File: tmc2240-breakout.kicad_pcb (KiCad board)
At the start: 2 copper layers, 69 x 51 mm, 0 parts

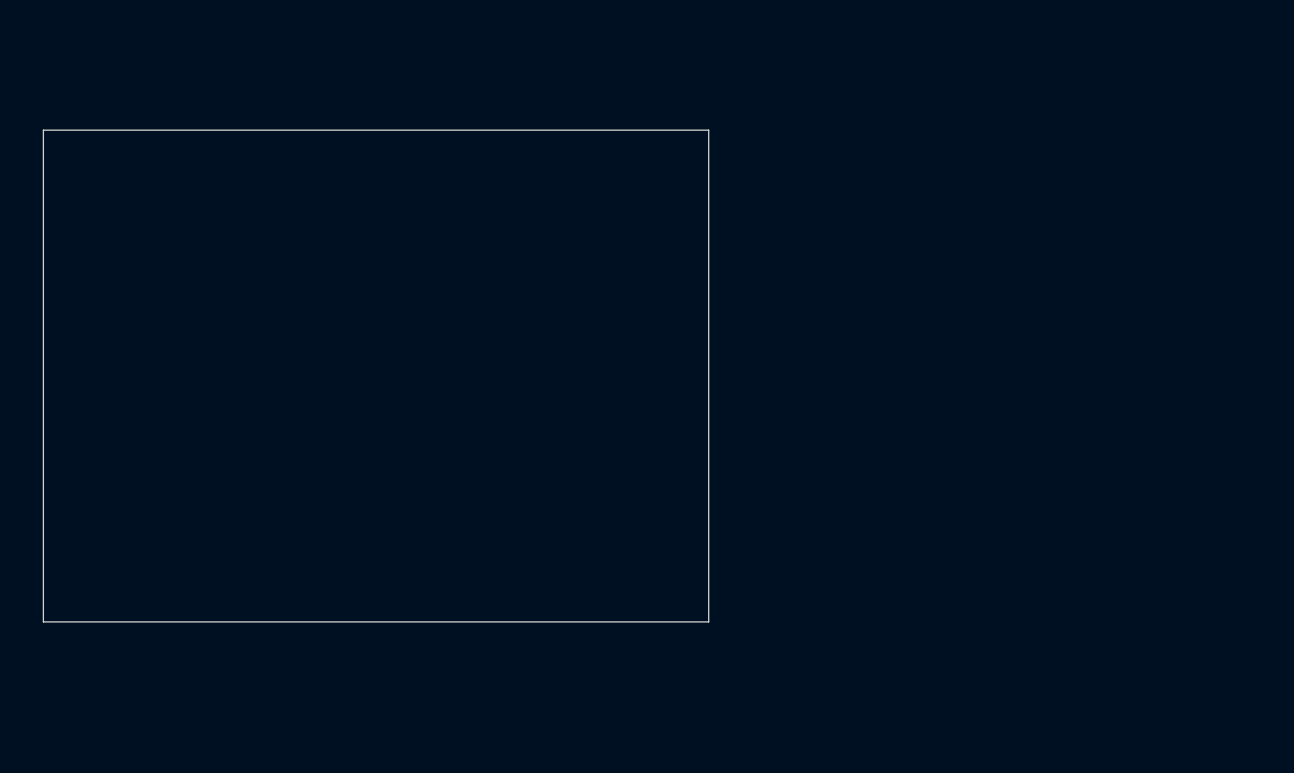
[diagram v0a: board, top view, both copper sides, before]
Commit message: did some pcb placement
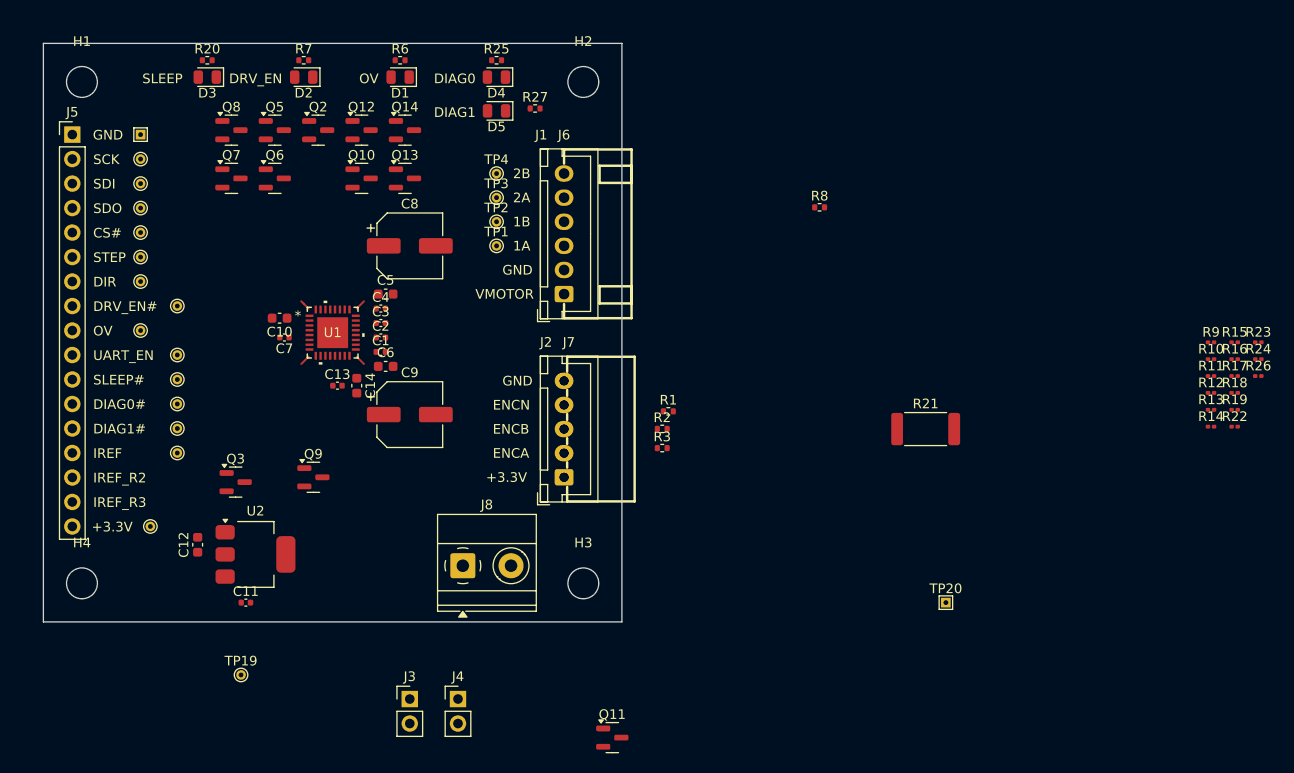
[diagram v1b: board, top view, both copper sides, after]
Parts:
- added C1: 100nF 50V, Capacitor_SMD:C_0402_1005Metric, F.Cu at (151.0, 92.0)
- added C10: 2.2uF 16V, Capacitor_SMD:C_0603_1608Metric, F.Cu at (140.5, 88.5)
- added C11: 100nF 50V, Capacitor_SMD:C_0402_1005Metric, F.Cu at (137.0, 118.0)
- added C12: 10uF 10V, Capacitor_SMD:C_0603_1608Metric, F.Cu at (132.0, 112.0)
- added C13: 22nF 50V, Capacitor_SMD:C_0402_1005Metric, F.Cu at (146.5, 95.5)
- added C14: 1uF 50V, Capacitor_SMD:C_0603_1608Metric, F.Cu at (148.5, 95.5)
- added C2: 100nF 50V, Capacitor_SMD:C_0402_1005Metric, F.Cu at (151.0, 90.5)
- added C3: 100nF 50V, Capacitor_SMD:C_0402_1005Metric, F.Cu at (151.0, 89.0)
- added C4: 100nF 50V, Capacitor_SMD:C_0402_1005Metric, F.Cu at (151.0, 87.5)
- added C5: 1uF 50V, Capacitor_SMD:C_0603_1608Metric, F.Cu at (151.5, 86.0)
- added C6: 1uF 50V, Capacitor_SMD:C_0603_1608Metric, F.Cu at (151.5, 93.5)
- added C7: 100nF 50V, Capacitor_SMD:C_0402_1005Metric, F.Cu at (141.0, 90.5)
- added C8: 47uF 63V, Capacitor_SMD:CP_Elec_6.3x7.7, F.Cu at (154.0, 81.0)
- added C9: 47uF 63V, Capacitor_SMD:CP_Elec_6.3x7.7, F.Cu at (154.0, 98.5)
- added D1: RED, LED_SMD:LED_0805_2012Metric, F.Cu at (153.0, 63.5)
- added D2: GREEN, LED_SMD:LED_0805_2012Metric, F.Cu at (143.0, 63.5)
- added D3: WHITE, LED_SMD:LED_0805_2012Metric, F.Cu at (133.0, 63.5)
- added D4: RED, LED_SMD:LED_0805_2012Metric, F.Cu at (163.0, 63.5)
- added D5: RED, LED_SMD:LED_0805_2012Metric, F.Cu at (163.0, 67.0)
- added H1: MountingHole, MountingHole:MountingHole_3.2mm_M3, F.Cu at (120.0, 64.0)
- added H2: MountingHole, MountingHole:MountingHole_3.2mm_M3, F.Cu at (172.0, 64.0)
- added H3: MountingHole, MountingHole:MountingHole_3.2mm_M3, F.Cu at (172.0, 116.0)
- added H4: MountingHole, MountingHole:MountingHole_3.2mm_M3, F.Cu at (120.0, 116.0)
- added J1: Conn_01x06, XH-W-6A:CONN-TH_6P-P2.50_DEALON_XH-W-6A, F.Cu at (170.0, 79.8)
- added J2: Conn_01x05, HDGC2501WR-5P:CONN-TH_5P-P2.50_HDGC2501WR-5P, F.Cu at (170.0, 100.0)
- added J3: Conn_01x02, Connector_PinHeader_2.54mm:PinHeader_1x02_P2.54mm_Vertical, F.Cu at (154.0, 128.0)
- added J4: Conn_01x02, Connector_PinHeader_2.54mm:PinHeader_1x02_P2.54mm_Vertical, F.Cu at (159.0, 128.0)
- added J5: Conn_01x17, Connector_PinHeader_2.54mm:PinHeader_1x17_P2.54mm_Vertical, F.Cu at (119.0, 69.5)
- added J6: Conn_01x06, Connector_JST:JST_XH_B6B-XH-A_1x06_P2.50mm_Vertical, F.Cu at (170.0, 86.0)
- added J7: Conn_01x05, Connector_JST:JST_XH_B5B-XH-A_1x05_P2.50mm_Vertical, F.Cu at (170.0, 105.0)
- added J8: Conn_01x02, TerminalBlock_Phoenix:TerminalBlock_Phoenix_MKDS-1,5-2_1x02_P5.00mm_Horizontal, F.Cu at (159.5, 114.2)
- added Q10: 2N7002, Package_TO_SOT_SMD:SOT-23, F.Cu at (149.0, 74.0)
- added Q11: 2N7002, Package_TO_SOT_SMD:SOT-23, F.Cu at (175.0, 132.0)
- added Q12: 2N7002, Package_TO_SOT_SMD:SOT-23, F.Cu at (149.0, 69.0)
- added Q13: 2N7002, Package_TO_SOT_SMD:SOT-23, F.Cu at (153.5, 74.0)
- added Q14: 2N7002, Package_TO_SOT_SMD:SOT-23, F.Cu at (153.5, 69.0)
- added Q2: 2N7002, Package_TO_SOT_SMD:SOT-23, F.Cu at (144.5, 69.0)
- added Q3: 2N7002, Package_TO_SOT_SMD:SOT-23, F.Cu at (135.9, 105.5)
- added Q5: 2N7002, Package_TO_SOT_SMD:SOT-23, F.Cu at (140.0, 69.0)
- added Q6: 2N7002, Package_TO_SOT_SMD:SOT-23, F.Cu at (140.0, 74.0)
- added Q7: 2N7002, Package_TO_SOT_SMD:SOT-23, F.Cu at (135.5, 74.0)
- added Q8: 2N7002, Package_TO_SOT_SMD:SOT-23, F.Cu at (135.5, 69.0)
- added Q9: 2N7002, Package_TO_SOT_SMD:SOT-23, F.Cu at (144.0, 105.0)
- added R1: 100k, Resistor_SMD:R_0402_1005Metric, F.Cu at (180.8, 98.2)
- added R10: 24k, Resistor_SMD:R_0201_0603Metric, F.Cu at (237.1, 92.8)
- added R11: 24k, Resistor_SMD:R_0201_0603Metric, F.Cu at (237.1, 94.5)
- added R12: 24k, Resistor_SMD:R_0201_0603Metric, F.Cu at (237.1, 96.2)
- added R13: 24k, Resistor_SMD:R_0201_0603Metric, F.Cu at (237.1, 98.0)
- added R14: 24k, Resistor_SMD:R_0201_0603Metric, F.Cu at (237.1, 99.8)
- added R15: 24k, Resistor_SMD:R_0201_0603Metric, F.Cu at (239.6, 91.0)
- added R16: 24k, Resistor_SMD:R_0201_0603Metric, F.Cu at (239.6, 92.8)
- added R17: 24k, Resistor_SMD:R_0201_0603Metric, F.Cu at (239.6, 94.5)
- added R18: 24k, Resistor_SMD:R_0201_0603Metric, F.Cu at (239.6, 96.2)
- added R19: 24k, Resistor_SMD:R_0201_0603Metric, F.Cu at (239.6, 98.0)
- added R2: 100k, Resistor_SMD:R_0402_1005Metric, F.Cu at (180.2, 100.0)
- added R20: 22, Resistor_SMD:R_0402_1005Metric, F.Cu at (133.0, 61.8)
- added R21: 1.8k, Resistor_SMD:R_2512_6332Metric, F.Cu at (207.5, 100.0)
- added R22: 24k, Resistor_SMD:R_0201_0603Metric, F.Cu at (239.6, 99.8)
- added R23: 24k, Resistor_SMD:R_0201_0603Metric, F.Cu at (242.0, 91.0)
- added R24: 24k, Resistor_SMD:R_0201_0603Metric, F.Cu at (242.0, 92.8)
- added R25: 33, Resistor_SMD:R_0402_1005Metric, F.Cu at (163.0, 61.8)
- added R26: 24k, Resistor_SMD:R_0201_0603Metric, F.Cu at (242.0, 94.5)
- added R27: 33, Resistor_SMD:R_0402_1005Metric, F.Cu at (167.0, 66.8)
- added R3: 100k, Resistor_SMD:R_0402_1005Metric, F.Cu at (180.2, 102.0)
- added R6: 33, Resistor_SMD:R_0402_1005Metric, F.Cu at (153.0, 61.8)
- added R7: 33, Resistor_SMD:R_0402_1005Metric, F.Cu at (143.0, 61.8)
- added R8: 100k, Resistor_SMD:R_0402_1005Metric, F.Cu at (196.5, 77.0)
- added R9: 24k, Resistor_SMD:R_0201_0603Metric, F.Cu at (237.1, 91.0)
- added TP1: TestPoint, TestPoint:TestPoint_THTPad_D1.0mm_Drill0.5mm, F.Cu at (163.0, 81.0)
- added TP10: TestPoint, TestPoint:TestPoint_THTPad_D1.0mm_Drill0.5mm, F.Cu at (126.1, 84.7)
- added TP11: TestPoint, TestPoint:TestPoint_THTPad_D1.0mm_Drill0.5mm, F.Cu at (129.9, 87.2)
- added TP12: TestPoint, TestPoint:TestPoint_THTPad_D1.0mm_Drill0.5mm, F.Cu at (126.1, 89.8)
- added TP13: TestPoint, TestPoint:TestPoint_THTPad_D1.0mm_Drill0.5mm, F.Cu at (129.9, 92.3)
- added TP14: TestPoint, TestPoint:TestPoint_THTPad_D1.0mm_Drill0.5mm, F.Cu at (129.9, 94.9)
- added TP15: TestPoint, TestPoint:TestPoint_THTPad_D1.0mm_Drill0.5mm, F.Cu at (129.9, 97.4)
- added TP16: TestPoint, TestPoint:TestPoint_THTPad_D1.0mm_Drill0.5mm, F.Cu at (129.9, 99.9)
- added TP17: TestPoint, TestPoint:TestPoint_THTPad_D1.0mm_Drill0.5mm, F.Cu at (129.9, 102.5)
- added TP18: TestPoint, TestPoint:TestPoint_THTPad_D1.0mm_Drill0.5mm, F.Cu at (127.1, 110.1)
- added TP19: TestPoint, TestPoint:TestPoint_THTPad_D1.0mm_Drill0.5mm, F.Cu at (136.5, 125.5)
- added TP2: TestPoint, TestPoint:TestPoint_THTPad_D1.0mm_Drill0.5mm, F.Cu at (163.0, 78.5)
- added TP20: TestPoint_Alt, TestPoint:TestPoint_THTPad_1.0x1.0mm_Drill0.5mm, F.Cu at (209.6, 118.0)
- added TP21: TestPoint_Alt, TestPoint:TestPoint_THTPad_1.0x1.0mm_Drill0.5mm, F.Cu at (126.1, 69.5)
- added TP3: TestPoint, TestPoint:TestPoint_THTPad_D1.0mm_Drill0.5mm, F.Cu at (163.0, 76.0)
- added TP4: TestPoint, TestPoint:TestPoint_THTPad_D1.0mm_Drill0.5mm, F.Cu at (163.0, 73.5)
- added TP5: TestPoint, TestPoint:TestPoint_THTPad_D1.0mm_Drill0.5mm, F.Cu at (126.1, 72.0)
- added TP6: TestPoint, TestPoint:TestPoint_THTPad_D1.0mm_Drill0.5mm, F.Cu at (126.1, 74.5)
- added TP7: TestPoint, TestPoint:TestPoint_THTPad_D1.0mm_Drill0.5mm, F.Cu at (126.1, 77.1)
- added TP8: TestPoint, TestPoint:TestPoint_THTPad_D1.0mm_Drill0.5mm, F.Cu at (126.1, 79.6)
- added TP9: TestPoint, TestPoint:TestPoint_THTPad_D1.0mm_Drill0.5mm, F.Cu at (126.1, 82.2)
- added U1: TMC2240ATJ+, ul_TMC2240ATJ-:21-0140_T3255&plus_5C_TRI, F.Cu at (146.0, 90.0)
- added U2: LD1117S18TR_SOT223, Package_TO_SOT_SMD:SOT-223-3_TabPin2, F.Cu at (138.0, 113.0)
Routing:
- net (no net): track 0.00 -> 4.24 mm
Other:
- board size 69 x 51 mm -> 60 x 60 mm
- board text added: "+3.3V"
- board text added: "1A"
- board text added: "1B"
- board text added: "2A"
- board text added: "2B"
- board text added: "CS#"
- board text added: "DIAG0"
- board text added: "DIAG0#"
- board text added: "DIAG1"
- board text added: "DIAG1#"
- board text added: "DIR"
- board text added: "DRV_EN"
- board text added: "DRV_EN#"
- board text added: "ENCA"
- board text added: "ENCB"
- board text added: "ENCN"
- board text added: "GND"
- board text added: "IREF"
- board text added: "IREF_R2"
- board text added: "IREF_R3"
- board text added: "OV"
- board text added: "SCK"
- board text added: "SDI"
- board text added: "SDO"
- board text added: "SLEEP"
- board text added: "SLEEP#"
- board text added: "STEP"
- board text added: "UART_EN"
- board text added: "VMOTOR"

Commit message: did some more placements
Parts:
- moved R19 110.0 mm to (132.2, 74.0)
- moved R12 104.1 mm to (133.0, 94.8), turned to 180 degrees
- moved R9 104.1 mm to (133.0, 89.8), turned to 180 degrees
- moved R11 104.1 mm to (133.0, 93.5)
- moved R10 104.1 mm to (133.0, 92.2), turned to 180 degrees
- moved R26 98.6 mm to (145.8, 73.0)
- moved R24 98.1 mm to (145.8, 74.0)
- moved R18 96.2 mm to (145.8, 75.0)
- moved R23 94.2 mm to (149.5, 109.0), turned to 90 degrees
- moved R16 91.8 mm to (148.8, 106.0), turned to 90 degrees
- moved R15 89.6 mm to (151.2, 106.0), turned to -90 degrees
- moved R13 87.5 mm to (150.0, 106.0), turned to -90 degrees
- moved R17 86.6 mm to (153.8, 106.0), turned to -90 degrees
- moved R14 84.8 mm to (152.5, 106.0), turned to -90 degrees
- moved R22 84.6 mm to (155.5, 109.0), turned to 90 degrees
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
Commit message: started doing some routing
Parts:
- moved R12 21.8 mm to (132.2, 73.0), turned to 0 degrees
- moved R9 11.2 mm to (133.0, 101.0)
- moved TP19 10.7 mm to (133.5, 107.1)
- moved C5 8.51 mm to (151.0, 94.5)
- moved C6 8.02 mm to (151.0, 85.5)
- moved C9 5.30 mm to (157.8, 102.2), turned to 180 degrees
- moved C8 5.15 mm to (149.0, 79.8)
- moved TP11 3.78 mm to (126.1, 87.2)
- moved R8 3.21 mm to (133.0, 90.2)
- moved R3 2.40 mm to (163.7, 90.5)
- moved TP5 1.81 mm to (127.9, 72.0)
- moved R1 1.30 mm to (165.1, 90.5)
- moved C1 1.15 mm to (151.0, 93.2)
- moved R10 0.71 mm to (133.0, 93.0)
- moved R11 0.71 mm to (133.0, 94.2)
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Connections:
- J1 pad 3: /OUT1A -> /OUT1B
- J1 pad 4: /OUT1B -> /OUT2B
- J1 pad 6: /OUT2B -> /OUT1A
- J5 pad 10: /UART_EN -> /DRV_EN#
- J5 pad 11: /SLEEP# -> /UART_EN
- J5 pad 14: /IREF -> /OV
- J5 pad 2: /SPI_SCK -> /SLEEP#
- J5 pad 3: /SPI_SDI -> /SPI_CS#
- J5 pad 4: /SPI_SDO -> /SPI_SCK
- J5 pad 5: /SPI_CS# -> /SPI_SDI
- J5 pad 6: /STEP -> /SPI_SDO
- J5 pad 7: /DIR -> /STEP
- J5 pad 8: /DRV_EN# -> /DIR
- J5 pad 9: /OV -> /IREF
- J6 pad 3: /OUT1A -> /OUT1B
- J6 pad 4: /OUT1B -> /OUT2B
- J6 pad 6: /OUT2B -> /OUT1A
- Q7 pad 1: /SLEEP_EN# -> /SLEEP#
- TP1 pad 1: /OUT1A -> /OUT1B
- TP10 pad 1: /DIR -> /STEP
- TP11 pad 1: /DRV_EN# -> /DIR
- TP12 pad 1: /OV -> /IREF
- TP13 pad 1: /UART_EN -> /DRV_EN#
- TP14 pad 1: /SLEEP# -> /UART_EN
- TP17 pad 1: /IREF -> /OV
- TP2 pad 1: /OUT1B -> /OUT2B
- TP4 pad 1: /OUT2B -> /OUT1A
- TP5 pad 1: /SPI_SCK -> /SLEEP#
- TP6 pad 1: /SPI_SDI -> /SPI_CS#
- TP7 pad 1: /SPI_SDO -> /SPI_SCK
- TP8 pad 1: /SPI_CS# -> /SPI_SDI
- TP9 pad 1: /STEP -> /SPI_SDO
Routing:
- net /SLEEP#: track 0.00 -> 41.0 mm
- net /ENCN: track 0.00 -> 35.7 mm, vias 0 -> 3
- net /SPI_CS#: track 0.00 -> 34.0 mm
- net /ENCB: track 0.00 -> 33.2 mm, vias 0 -> 3
- net /OV: track 0.00 -> 32.7 mm
- net /ENCA: track 0.00 -> 32.7 mm, vias 0 -> 3
- net /SPI_SCK: track 0.00 -> 32.5 mm
- net /SPI_SDI: track 0.00 -> 30.9 mm
- net /DIAG1#: track 0.00 -> 30.2 mm
- net /SPI_SDO: track 0.00 -> 29.4 mm
- net /DRV_EN#: track 0.00 -> 29.4 mm
- net /UART_EN: track 0.00 -> 29.1 mm
- net /DIAG0#: track 0.00 -> 28.7 mm
- net /STEP: track 0.00 -> 27.3 mm
- net /DIR: track 0.00 -> 26.4 mm
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- added copper zone on F.Cu, net +3.3V
- added copper zone on F.Cu, net /OUT1A
- added copper zone on F.Cu, net /OUT1B
- added copper zone on F.Cu, net /OUT2A
- added copper zone on F.Cu, net /OUT2B
- added copper zone on B.Cu, net GND
- added copper zone on F.Cu, net GND
- added copper zone on B.Cu, net VMOTOR
- added copper zone on F.Cu, net VMOTOR
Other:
- board text added: "TODO: Motor pin labels are wrong"

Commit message: trying to export 3d model
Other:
- board text added: "PCB3D_BR_BOARD"
- board text added: "PCB3D_TL_BOARD"
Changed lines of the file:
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@@
+		)
+	)
+	(gr_text "PCB3D_BR_BOARD"
+		(at 176 119.96 0)
+		(layer "User.1")
+		(effects
+			(font
+				(size 1 1)
+				(thickness 0.15)
+			)
+			(justify left bottom)
+		)
+	)
+	(gr_text "PCB3D_TL_BOARD"
+		(at 116 59.96 0)
+		(layer "User.1")
+		(effects
+			(font
+				(size 1 1)
+				(thickness 0.15)
+			)
+			(justify left bottom)
 		)
 	)

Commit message: did some more pcb layout
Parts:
- moved R2 23.0 mm to (145.2, 100.0), turned to -90 degrees
- moved R3 21.8 mm to (144.0, 100.0), turned to -90 degrees
- moved R1 20.8 mm to (146.5, 100.0), turned to -90 degrees
- moved C12 6.89 mm to (137.8, 108.2), turned to 180 degrees
- turned C8 to 180 degrees
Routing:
- net Net-(Q3-D): track 0.00 -> 6.48 mm
- net /IREF_R3: track 0.00 -> 5.72 mm
- net /IREF_R2: track 0.00 -> 5.72 mm
- net Net-(Q11-D): track 0.00 -> 3.38 mm
- net /ENCA: track 32.7 -> 35.4 mm
- net /IREF: track 25.8 -> 28.3 mm
- net /ENCB: track 33.2 -> 35.3 mm
- net Net-(R14-Pad2): track 0.00 -> 1.52 mm
- net Net-(R13-Pad2): track 0.00 -> 1.25 mm
- net /ENCN: track 35.7 -> 36.9 mm
- added copper zone on F.Cu, net +1V8

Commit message: did some more pcb layout
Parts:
- moved Q9 25.8 mm to (132.8, 79.8)
- moved R21 19.8 mm to (139.5, 79.8), turned to 180 degrees
- moved TP19 9.06 mm to (142.2, 104.8)
- moved C12 2.00 mm to (139.8, 108.2)
- turned C8 to 0 degrees
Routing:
- net /SLEEP#: track 41.0 -> 50.3 mm
- net /SPI_CS#: track 34.0 -> 38.6 mm
- net /SPI_SCK: track 32.5 -> 35.8 mm
- net /SPI_SDI: track 30.9 -> 33.0 mm
- net /SPI_SDO: track 29.4 -> 30.2 mm
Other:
- board text added: "+1.8V"

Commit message: old commit
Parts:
- moved TP19 2.51 mm to (139.8, 105.0)
- moved J3 2.00 mm to (149.0, 116.0)
- moved Q3 1.00 mm to (148.0, 109.0)
- moved R23 1.00 mm to (150.5, 109.0)
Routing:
- net GND: track 2.50 -> 16.2 mm, vias 5 -> 14
- net Net-(Q3-D): track 6.48 -> 0.00 mm
- net /IREF_R2: track 5.72 -> 1.82 mm
